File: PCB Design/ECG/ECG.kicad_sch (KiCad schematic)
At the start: 3 parts, among them U1 RT5760A, U2 TP4056M

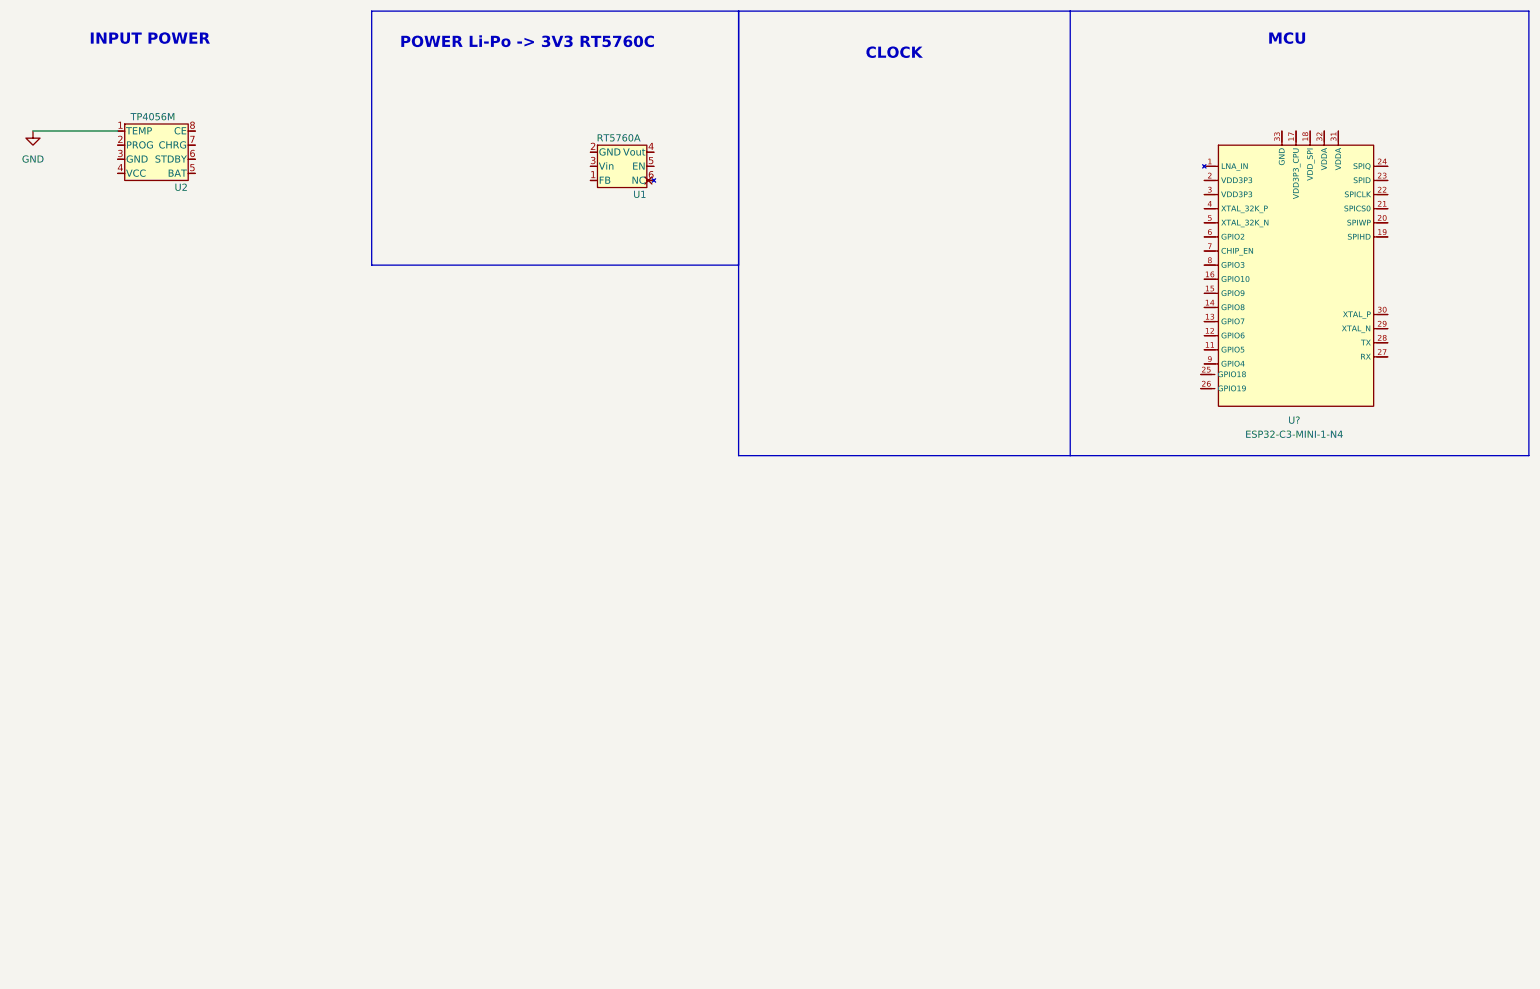
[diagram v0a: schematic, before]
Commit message: Continued work
added buck converter and switch footprint
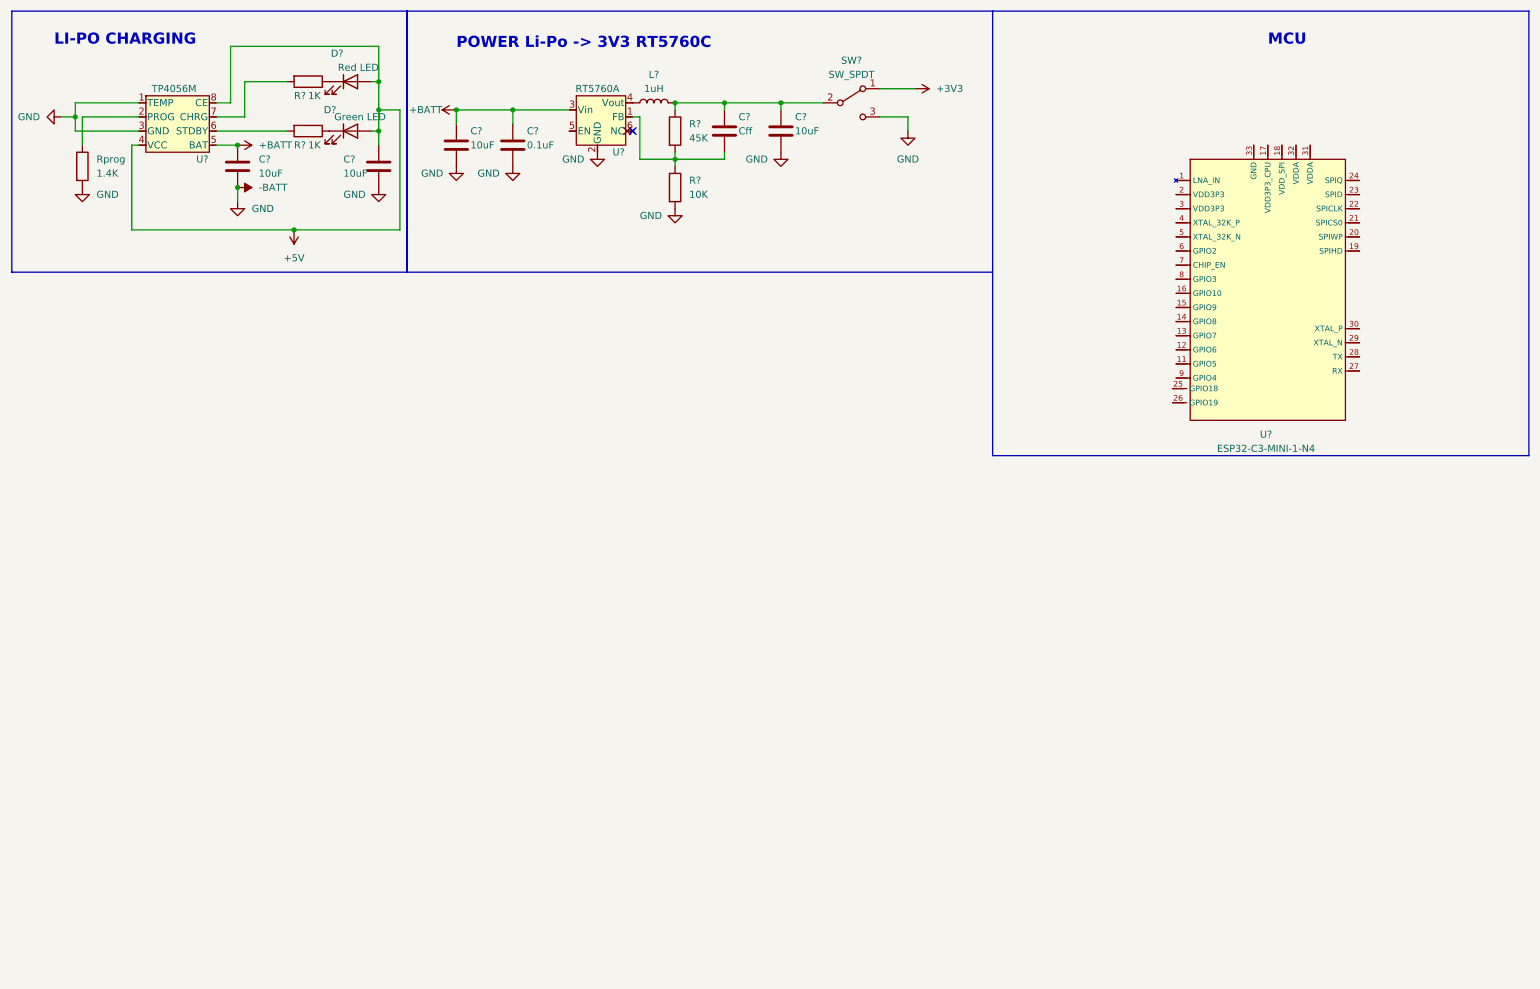
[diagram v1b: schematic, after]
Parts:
- added C? (x4): 10uF, symbol Device:C
- added C?: Cff, symbol Device:C
- added C?: 0.1uF, symbol Device:C
- added D?: Red LED, symbol Device:LED
- added D?: Green LED, symbol Device:LED
- added L?: 1uH, symbol Device:L
- added R? (x2): 1K, symbol Device:R
- added R?: 45K, symbol Device:R
- added R?: 10K, symbol Device:R
- added Rprog: 1.4K, symbol Device:R
- added SW?: SW_SPDT, SS-12D02-VG4:SS-12D02-VG4, symbol Switch:SW_SPDT
- renumbered U1 to U?, U2 to U?
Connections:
- net GND is gone; now on net -BATT: U?.1 (TEMP)
- net at U?.1 (FB): now also C?.2, R?.1, R?.2
- net -BATT: now reaches U?.2 (GND)
- net -BATT: now also U?.3 (GND), C?.2, C?.2, C?.2, C?.2, C?.2, R?.2, Rprog.2, SW?.3 (C)
- net +BATT: now reaches U?.3 (Vin)
- net +BATT: now also U?.5 (BAT), C?.1, C?.1, C?.1
- net at U?.4 (Vout): now also L?.1
- net at U?.2 (PROG): now also Rprog.1
- net +5V: now reaches U?.4 (VCC)
- net +5V: now also U?.8 (CE), C?.1, D?.2 (A), D?.2 (A)
- net at U?.6 (STDBY): now also R?.2
- net at U?.7 (CHRG): now also R?.2
- new net: C?.1, C?.1, L?.2, R?.1, SW?.2 (B)
- new net: D?.1 (K), R?.1 (x2)
- new net +3V3: SW?.1 (A)
- no-connect marks 0 -> 1
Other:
- note added: "LI-PO CHARGING"
- note removed: "CLOCK"
- note removed: "INPUT POWER"
- moved on the sheet: U?

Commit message: Updates to schematic
Correct and added MCU
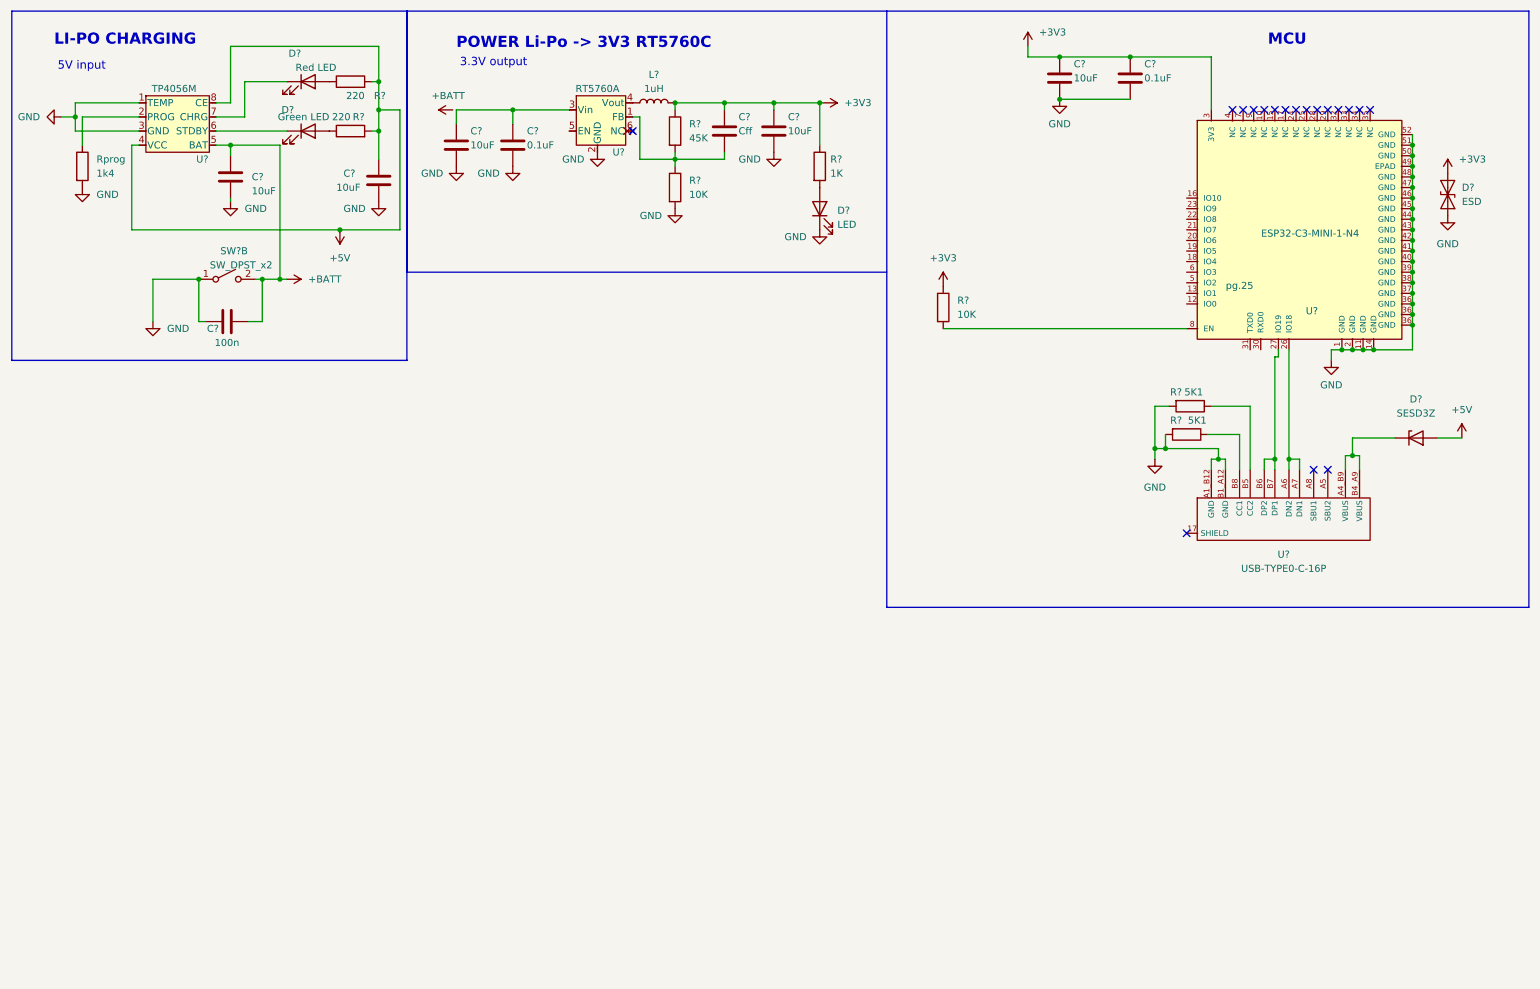
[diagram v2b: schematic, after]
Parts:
- removed SW?: SW_SPDT, SS-12D02-VG4:SS-12D02-VG4, symbol Switch:SW_SPDT
- added C?: 0.1uF, symbol Device:C
- added C?: 10uF, symbol Device:C
- added C?: 100n, symbol Device:C
- added D?: ESD, Diode_SMD:D_SOD-923, symbol Diode:ESD9B3.3ST5G
- added D?: LED, symbol Device:LED
- added D?: SESD3Z, Diode_SMD:D_SOD-323_HandSoldering, symbol Diode:ESD5Zxx
- added R? (x2): 5K1, symbol Device:R
- added R?: 1K, symbol Device:R
- added R?: 10K, symbol Device:R
- added SW?: SW_DPST_x2, SS-12D02-VG4:SS-12D02-VG4, symbol Switch:SW_DPST_x2
- added U?: USB-TYPE0-C-16P, symbol USB-TYPE-C-16P:USB-TYPE0-C-16P
- R? (x2): value 1K -> 220
- Rprog: value 1.4K -> 1k4
- U?: STANDARD (none) -> pg.25
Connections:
- net -BATT is gone; now on net GND: C?.2, C?.2, C?.2, C?.2, C?.2, R?.2, Rprog.2, U?.1 (TEMP), U?.2 (GND), U?.3 (GND)
- net +3V3: now also C?.1, C?.1, L?.2, R?.1, U?.3 (3V3), C?.1, C?.1, D?.2 (A2), R?.1, R?.1
- net +5V: now also R?.2, R?.2, D?.2 (A); no longer D?.2 (A), D?.2 (A)
- net +BATT: now also C?.2, SW?.2 (B); no longer C?.1, C?.1, U?.3 (Vin)
- net at D?.1 (K): now also U?.7 (CHRG); no longer R?.1
- net at D?.1 (K): now also U?.6 (STDBY); no longer R?.1
- net GND: now reaches U?.1 (GND)
- net GND: now also U?.11 (GND), U?.14 (GND), U?.2 (GND), U?.36 (GND), U?.37 (GND), U?.38 (GND), U?.39 (GND), U?.40 (GND), U?.41 (GND), U?.42 (GND), U?.43 (GND), U?.44 (GND), U?.45 (GND), U?.46 (GND), U?.47 (GND), U?.48 (GND), U?.49 (EPAD), U?.50 (GND), U?.51 (GND), U?.52 (GND), C?.1, C?.2, C?.2, D?.1 (A1), D?.1 (K), R?.2, R?.2, SW?.1 (A), U?.A1_B12 (GND), U?.B1_A12 (GND)
- net at U?.26 (IO18): now also U?.A6 (DN2), U?.A7 (DN1)
- net at U?.27 (IO19): now also U?.B6 (DP2), U?.B7 (DP1)
- net at U?.8 (EN): now also R?.2
- new net: R?.1, U?.B5 (CC2)
- new net: D?.2 (A), R?.1 (x2)
- new net: C?.1, C?.1, U?.3 (Vin)
- new net: D?.2 (A), R?.2
- new net: D?.1 (K), U?.A4_B9 (VBUS), U?.B4_A9 (VBUS)
- new net: R?.1, U?.B8 (CC1)
- no-connect marks 1 -> 18
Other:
- note added: "3.3V output"
- note added: "5V input"
- moved on the sheet: C?, D?, R?

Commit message: changes to pcb, added ad8232
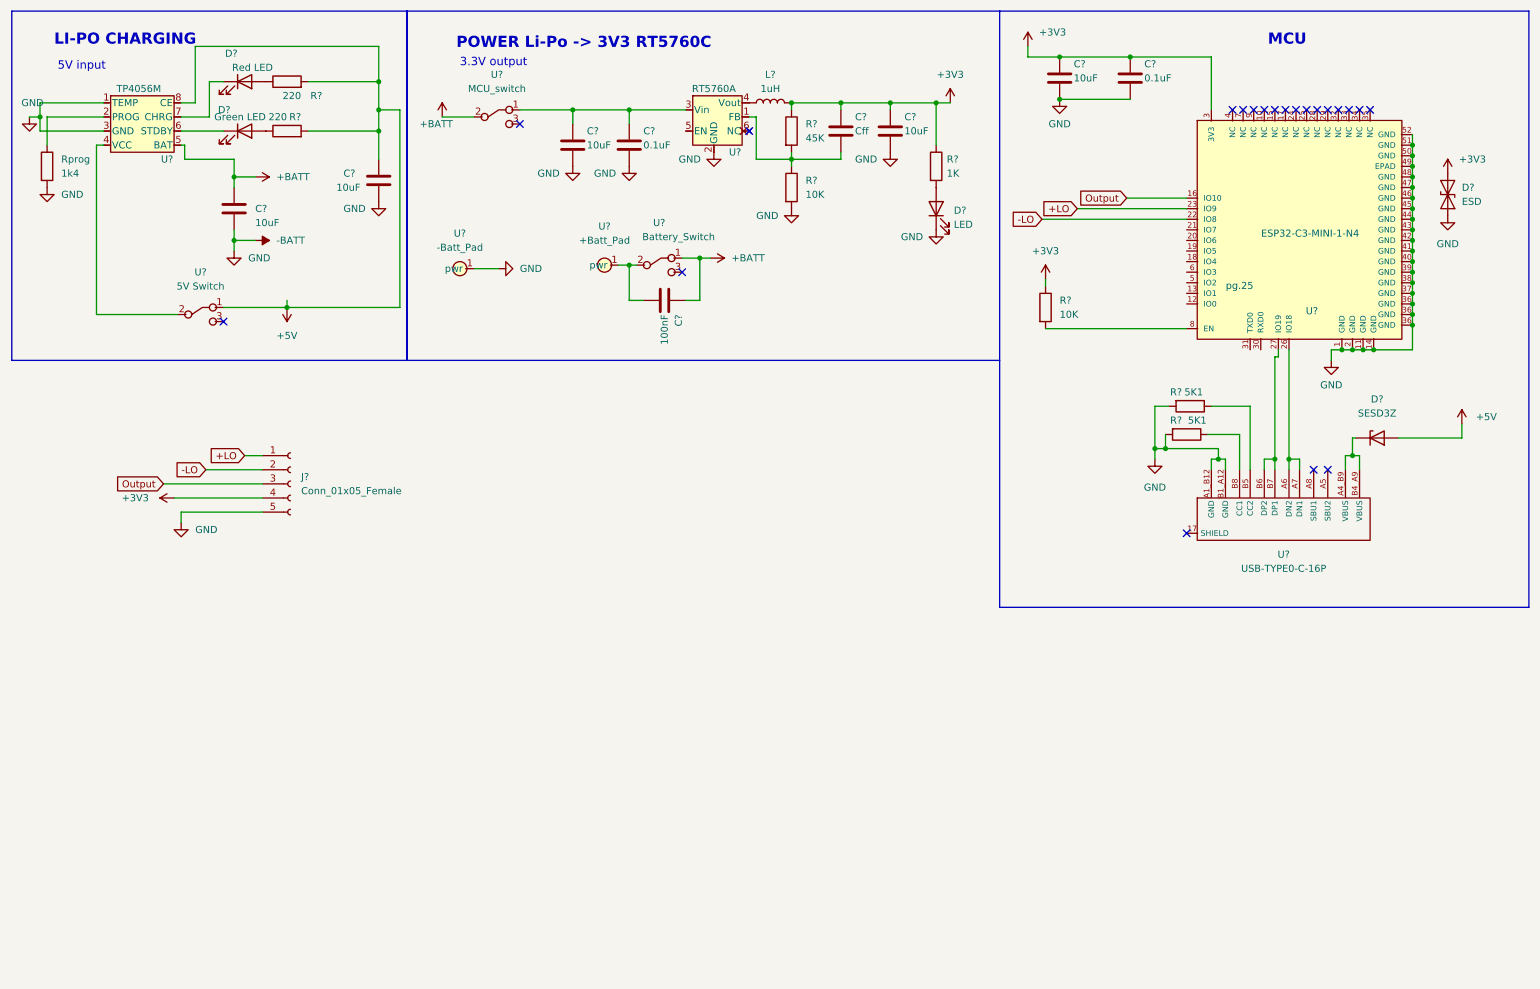
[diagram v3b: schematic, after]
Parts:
- removed C?: 100n, symbol Device:C
- removed SW?: SW_DPST_x2, SS-12D02-VG4:SS-12D02-VG4, symbol Switch:SW_DPST_x2
- added C?: 100nF, symbol Device:C
- added J?: Conn_01x05_Female, symbol Connector:Conn_01x05_Female
- added U?: +Batt_Pad, Single pad :sing pad, symbol Single_Pad:Single_pad
- added U?: 5V Switch, SS-12D02-VG4:SS-12D02-VG4, symbol battery switch:Battery_Switch
- added U?: -Batt_Pad, symbol Single_Pad:Single_pad
- added U?: MCU_switch, SS-12D02-VG4:SS-12D02-VG4, symbol battery switch:MCU_switch
- added U?: Battery_Switch, SS-12D02-VG4:SS-12D02-VG4, symbol battery switch:Battery_Switch
- U?: footprint (none) -> Package_TO_SOT_SMD:SOT-563
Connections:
- net +3V3: now also J?.4 (Pin_4)
- net +5V: now also U?.1; no longer U?.4 (VCC)
- net +BATT: now also C?.1, U?.1, U?.2
- net at C?.1, C?.1, U?.3 (Vin): now also U?.1
- net Output: now reaches U?.16 (IO10)
- net Output: now also J?.3 (Pin_3)
- net -LO: now reaches U?.22 (IO8)
- net -LO: now also J?.2 (Pin_2)
- net +LO: now reaches U?.23 (IO9)
- net +LO: now also J?.1 (Pin_1)
- net GND renamed -BATT
- net -BATT: now also J?.5 (Pin_5), U?.1 (pwr)
- new net: C?.2, U?.1 (pwr), U?.2
- new net: U?.2, U?.4 (VCC)
- no-connect marks 18 -> 21
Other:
- moved on the sheet: C?, D?, L?, R?, Rprog, U?

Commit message: changes to schematic of pcb
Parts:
- removed D?: ESD, Diode_SMD:D_SOD-923, symbol Diode:ESD9B3.3ST5G
- removed D?: SESD3Z, Diode_SMD:D_SOD-323_HandSoldering, symbol Diode:ESD5Zxx
- removed U?: +Batt_Pad, Single pad :sing pad, symbol Single_Pad:Single_pad
- removed U?: 5V Switch, SS-12D02-VG4:SS-12D02-VG4, symbol battery switch:Battery_Switch
- removed U?: -Batt_Pad, symbol Single_Pad:Single_pad
- removed U?: MCU_switch, SS-12D02-VG4:SS-12D02-VG4, symbol battery switch:MCU_switch
- added C?: 100nF, symbol Device:C
- added C?: 10uF, symbol Device:C
- added D?: Blue LED, LED_SMD:LED_0603_1608Metric, symbol Device:LED
- added R?: 220, symbol Device:R
- added R?: 10K, symbol Device:R
- added SW?: SW_Push, Buttons:Tactile_pushbutton_6x6mm, symbol Switch:SW_Push
- added U?: USBLC6-2SC6, Package_TO_SOT_SMD:SOT-23-6, symbol Power_Protection:USBLC6-2SC6
- added U?: MCU_switch, Switches:3V3 SWT, symbol battery switch:MCU_switch
- added U?: Li-Po, Battery_solder_pads:Battery Solder Pad 2.5x2.0mm, symbol Battery:Li-Po
- added U?: 3V3TP, symbol Test points:TP
- added U?: 5V Switch, Switches:5V, symbol battery switch:Battery_Switch
- D?: value Red LED -> RED
- J?: footprint (none) -> Connector_PinHeader_1.00mm:PinHeader_1x05_P1.00mm_Vertical
- R?: value 1K -> 220
- U?: footprint MSOP-8-1EP_3x3mm_P0.65mm_EP1.68x1.88mm -> Package_SO:MSOP-8-1EP_3x3mm_P0.65mm_EP2.5x3mm_Mask1.73x2.36mm_ThermalVias
- U?: footprint SS-12D02-VG4:SS-12D02-VG4 -> Switches:Battery_swt
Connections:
- net +3V3: now also C?.1, SW?.2, U?.
- net +5V: now also U?.A4_B9 (VBUS), U?.B4_A9 (VBUS), C?.1
- net +BATT: now also U?.2
- net -BATT: now also C?.2, D?.1 (K), R?.2, U?.2 (-Bat), U?.2 (GND)
- net +4V: now reaches C?.1, C?.1, U?.3 (Vin)
- net +4V: now also U?.1
- net BTN: now reaches U?.12 (IO0)
- net BTN: now also C?.2, R?.1, SW?.1
- net LED: now reaches U?.13 (IO1)
- net LED: now also R?.1
- net DN: now reaches U?.A6 (DN2), U?.A7 (DN1)
- net DN: now also U?.1 (I/O1); no longer U?.26 (IO18)
- net DP: now reaches U?.B6 (DP2), U?.B7 (DP1)
- net DP: now also U?.6 (I/O1); no longer U?.27 (IO19)
- net BatO: now reaches C?.2, U?.2
- net BatO: now also U?.1 (+Bat)
- net In_5V: now reaches U?.4 (VCC)
- net In_5V: now also U?.2
- new net: D?.2 (A), R?.2
- new net DNO: U?.26 (IO18), U?.3 (I/O2)
- new net DPO: U?.27 (IO19), U?.4 (I/O2)
- no-connect marks 21 -> 28
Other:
- note added: "AD8232"
- note added: "BUTTONS AND LED"
- note added: "Input"
- note added: "PROTECTION"
- note added: "SWITCHES AND SOLDER PNTS"
- moved on the sheet: C?, D?, J?, L?, R?, Rprog, U?
